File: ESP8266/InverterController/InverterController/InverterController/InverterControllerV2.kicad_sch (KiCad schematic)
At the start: 36 parts

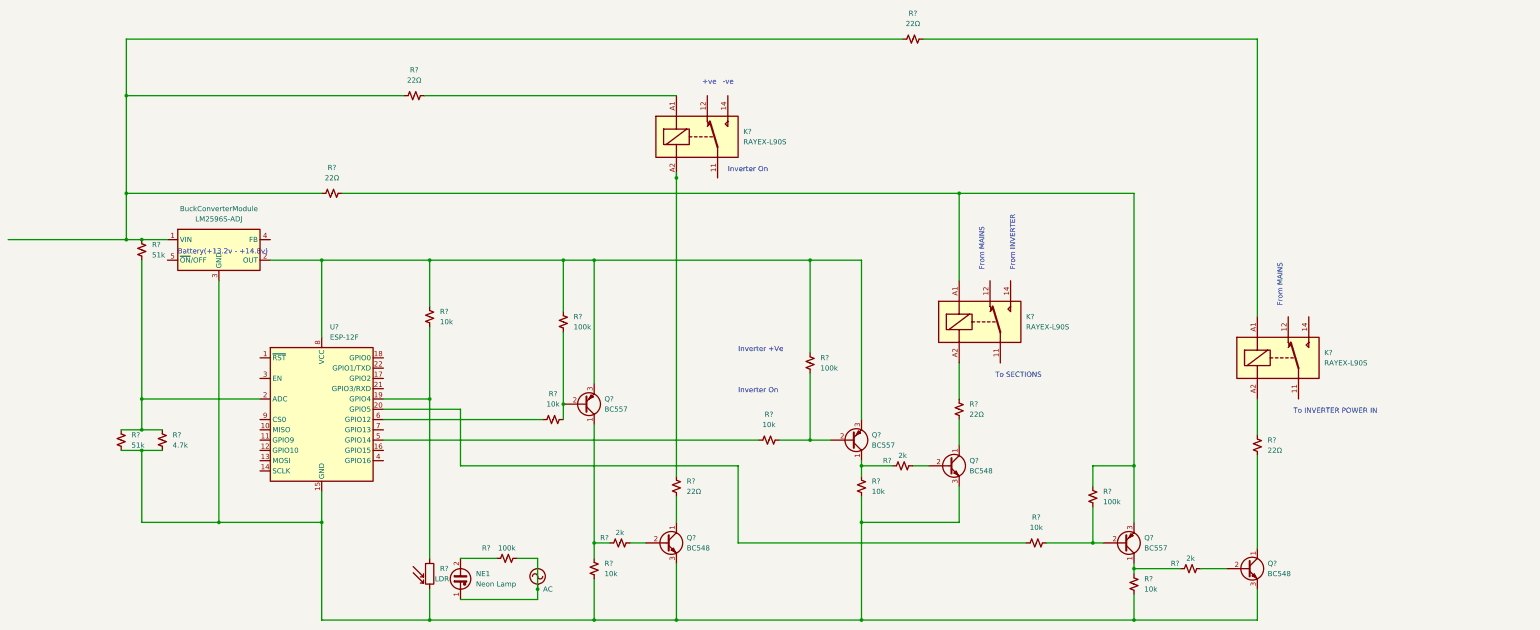
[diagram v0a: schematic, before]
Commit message: Design fixes to use a relays,code improvements and bug fixes, improvements for v2
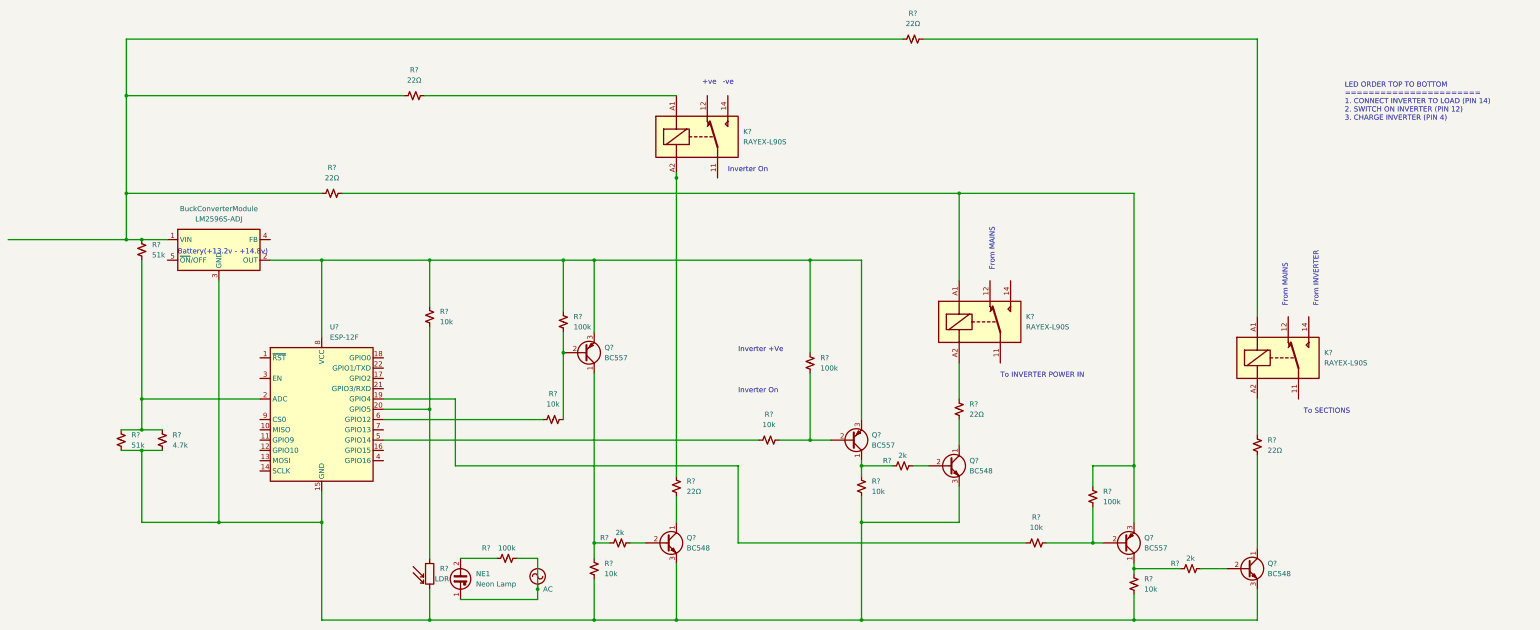
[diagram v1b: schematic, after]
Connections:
- net at R?.1, R?.2: now also U?.20 (GPIO5); no longer U?.19 (GPIO4)
- net at R?.1: now also U?.19 (GPIO4); no longer U?.20 (GPIO5)
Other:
- note added: "LED ORDER TOP TO BOTTOM ======================= 1. CONNECT INVERTER TO LOAD (PIN 14) 2. SWITCH ON INVERTER (PIN 12) 3. CHARGE INVERTER (PIN 4)"
- moved on the sheet: Q?
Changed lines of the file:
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@@
   (junction (at 95.25 157.48) (diameter 0) (color 0 0 0 0)
   )
+  (junction (at 154.94 115.57) (diameter 0) (color 0 0 0 0)
+  )
   (junction (at 162.56 181.61) (diameter 0) (color 0 0 0 0)
   )
@@
   (junction (at 50.8 139.7) (diameter 0) (color 0 0 0 0)
   )
-  (junction (at 154.94 128.27) (diameter 0) (color 0 0 0 0)
-  )
   (junction (at 228.6 143.51) (diameter 0) (color 0 0 0 0)
   )
-  (junction (at 121.92 127) (diameter 0) (color 0 0 0 0)
+  (junction (at 121.92 129.54) (diameter 0) (color 0 0 0 0)
   )
   (junction (at 215.9 137.16) (diameter 0) (color 0 0 0 0)
   )
+  (wire (pts (xy 110.49 127) (xy 128.27 127))
+    (stroke (width 0) (type default) (color 0 0 0 0))
+  )
   (wire (pts (xy 252.73 76.2) (xy 252.73 97.79))
     (stroke (width 0) (type default) (color 0 0 0 0))
@@
     (stroke (width 0) (type default) (color 0 0 0 0))
   )
-  (wire (pts (xy 198.12 143.51) (xy 129.54 143.51))
+  (wire (pts (xy 198.12 143.51) (xy 128.27 143.51))
     (stroke (width 0) (type default) (color 0 0 0 0))
   )
@@
     (stroke (width 0) (type default) (color 0 0 0 0))
   )
-  (wire (pts (xy 154.94 110.49) (xy 154.94 128.27))
+  (wire (pts (xy 154.94 110.49) (xy 154.94 115.57))
+    (stroke (width 0) (type default) (color 0 0 0 0))
+  )
+  (wire (pts (xy 154.94 115.57) (xy 154.94 132.08))
     (stroke (width 0) (type default) (color 0 0 0 0))
   )
@@
     (stroke (width 0) (type default) (color 0 0 0 0))
   )
-  (wire (pts (xy 162.56 92.71) (xy 162.56 123.19))
+  (wire (pts (xy 162.56 92.71) (xy 162.56 110.49))
     (stroke (width 0) (type default) (color 0 0 0 0))
   )
@@
     (stroke (width 0) (type default) (color 0 0 0 0))
   )
-  (wire (pts (xy 129.54 129.54) (xy 110.49 129.54))
-    (stroke (width 0) (type default) (color 0 0 0 0))
-  )
   (wire (pts (xy 162.56 92.71) (xy 215.9 92.71))
     (stroke (width 0) (type default) (color 0 0 0 0))
@@
     (stroke (width 0) (type default) (color 0 0 0 0))
   )
-  (wire (pts (xy 121.92 127) (xy 121.92 166.37))
+  (wire (pts (xy 121.92 109.22) (xy 121.92 129.54))
     (stroke (width 0) (type default) (color 0 0 0 0))
   )
@@
     (stroke (width 0) (type default) (color 0 0 0 0))
   )
-  (wire (pts (xy 162.56 133.35) (xy 162.56 162.56))
+  (wire (pts (xy 162.56 120.65) (xy 162.56 162.56))
     (stroke (width 0) (type default) (color 0 0 0 0))
   )
@@
     (stroke (width 0) (type default) (color 0 0 0 0))
   )
-  (wire (pts (xy 110.49 127) (xy 121.92 127))
-    (stroke (width 0) (type default) (color 0 0 0 0))
-  )
   (wire (pts (xy 182.88 167.64) (xy 182.88 181.61))
     (stroke (width 0) (type default) (color 0 0 0 0))
@@
     (stroke (width 0) (type default) (color 0 0 0 0))
   )
+  (wire (pts (xy 110.49 129.54) (xy 121.92 129.54))
+    (stroke (width 0) (type default) (color 0 0 0 0))
+  )
   (wire (pts (xy 215.9 137.16) (xy 220.98 137.16))
     (stroke (width 0) (type default) (color 0 0 0 0))
@@
     (stroke (width 0) (type default) (color 0 0 0 0))
   )
+  (wire (pts (xy 121.92 129.54) (xy 121.92 166.37))
+    (stroke (width 0) (type default) (color 0 0 0 0))
+  )
   (wire (pts (xy 46.99 52.07) (xy 46.99 38.1))
     (stroke (width 0) (type default) (color 0 0 0 0))
@@
     (stroke (width 0) (type default) (color 0 0 0 0))
   )
-  (wire (pts (xy 121.92 109.22) (xy 121.92 127))
-    (stroke (width 0) (type default) (color 0 0 0 0))
-  )
   (wire (pts (xy 274.32 162.56) (xy 285.75 162.56))
     (stroke (width 0) (type default) (color 0 0 0 0))
@@
     (stroke (width 0) (type default) (color 0 0 0 0))
   )
-  (wire (pts (xy 129.54 143.51) (xy 129.54 129.54))
+  (wire (pts (xy 128.27 127) (xy 128.27 143.51))
     (stroke (width 0) (type default) (color 0 0 0 0))
   )
@@
     (stroke (width 0) (type default) (color 0 0 0 0))
   )
-  (wire (pts (xy 154.94 128.27) (xy 154.94 132.08))
-    (stroke (width 0) (type default) (color 0 0 0 0))
-  )
   (wire (pts (xy 110.49 137.16) (xy 203.2 137.16))
     (stroke (width 0) (type default) (color 0 0 0 0))
@@
     (effects (font (size 1.27 1.27)) (justify left bottom))
   )
-  (text "From MAINS" (at 332.74 104.14 90)
-    (effects (font (size 1.27 1.27)) (justify left bottom))
-  )
-  (text "From INVERTER" (at 266.7 95.25 90)
+  (text "From MAINS" (at 261.62 95.25 90)
+    (effects (font (size 1.27 1.27)) (justify left bottom))
+  )
+  (text "LED ORDER TOP TO BOTTOM\n=======================\n1. CONNECT INVERTER TO LOAD (PIN 14)\n2. SWITCH ON INVERTER (PIN 12)\n3. CHARGE INVERTER (PIN 4)\n"
+    (at 347.98 58.42 0)
+    (effects (font (size 1.27 1.27)) (justify left bottom))
+  )
+  (text "From INVERTER" (at 341.63 104.14 90)
     (effects (font (size 1.27 1.27)) (justify left bottom))
   )
@@
     (effects (font (size 1.27 1.27)) (justify left bottom))
   )
-  (text "From MAINS" (at 259.08 95.25 90)
-    (effects (font (size 1.27 1.27)) (justify left bottom))
-  )
-  (text "To SECTIONS" (at 261.62 121.92 0)
+  (text "From MAINS" (at 334.01 104.14 90)
+    (effects (font (size 1.27 1.27)) (justify left bottom))
+  )
+  (text "To SECTIONS" (at 337.82 130.81 0)
     (effects (font (size 1.27 1.27)) (justify left bottom))
   )
@@
     (effects (font (size 1.27 1.27)) (justify left bottom))
   )
-  (text "To INVERTER POWER IN" (at 335.28 130.81 0)
+  (text "To INVERTER POWER IN" (at 262.89 121.92 0)
     (effects (font (size 1.27 1.27)) (justify left bottom))
   )
@@
     (pin "2")
   )
-  (symbol (lib_id "Transistor_BJT:BC557") (at 160.02 128.27 0) (mirror x) (unit 1)
-    (in_bom yes) (on_board yes) (fields_autoplaced)
-    (property "Reference" "Q?" (id 0) (at 165.1 126.9999 0)
-      (effects (font (size 1.27 1.27)) (justify left))
-    )
-    (property "Value" "BC557" (id 1) (at 165.1 129.5399 0)
-      (effects (font (size 1.27 1.27)) (justify left))
-    )
-    (property "Footprint" "Package_TO_SOT_THT:TO-92_Inline" (id 2) (at 165.1 126.365 0)
+  (symbol (lib_id "Transistor_BJT:BC557") (at 160.02 115.57 0) (mirror x) (unit 1)
+    (in_bom yes) (on_board yes) (fields_autoplaced)
+    (property "Reference" "Q?" (id 0) (at 165.1 114.2999 0)
+      (effects (font (size 1.27 1.27)) (justify left))
+    )
+    (property "Value" "BC557" (id 1) (at 165.1 116.8399 0)
+      (effects (font (size 1.27 1.27)) (justify left))
+    )
+    (property "Footprint" "Package_TO_SOT_THT:TO-92_Inline" (id 2) (at 165.1 113.665 0)
       (effects (font (size 1.27 1.27) italic) (justify left) hide)
     )
-    (property "Datasheet" "https://www.onsemi.com/pub/Collateral/BC556BTA-D.pdf" (id 3) (at 160.02 128.27 0)
+    (property "Datasheet" "https://www.onsemi.com/pub/Collateral/BC556BTA-D.pdf" (id 3) (at 160.02 115.57 0)
       (effects (font (size 1.27 1.27)) (justify left) hide)
     )
